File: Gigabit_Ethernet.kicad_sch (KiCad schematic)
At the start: 1 part, among them X800 ECS-2520MV-250-BN-TR

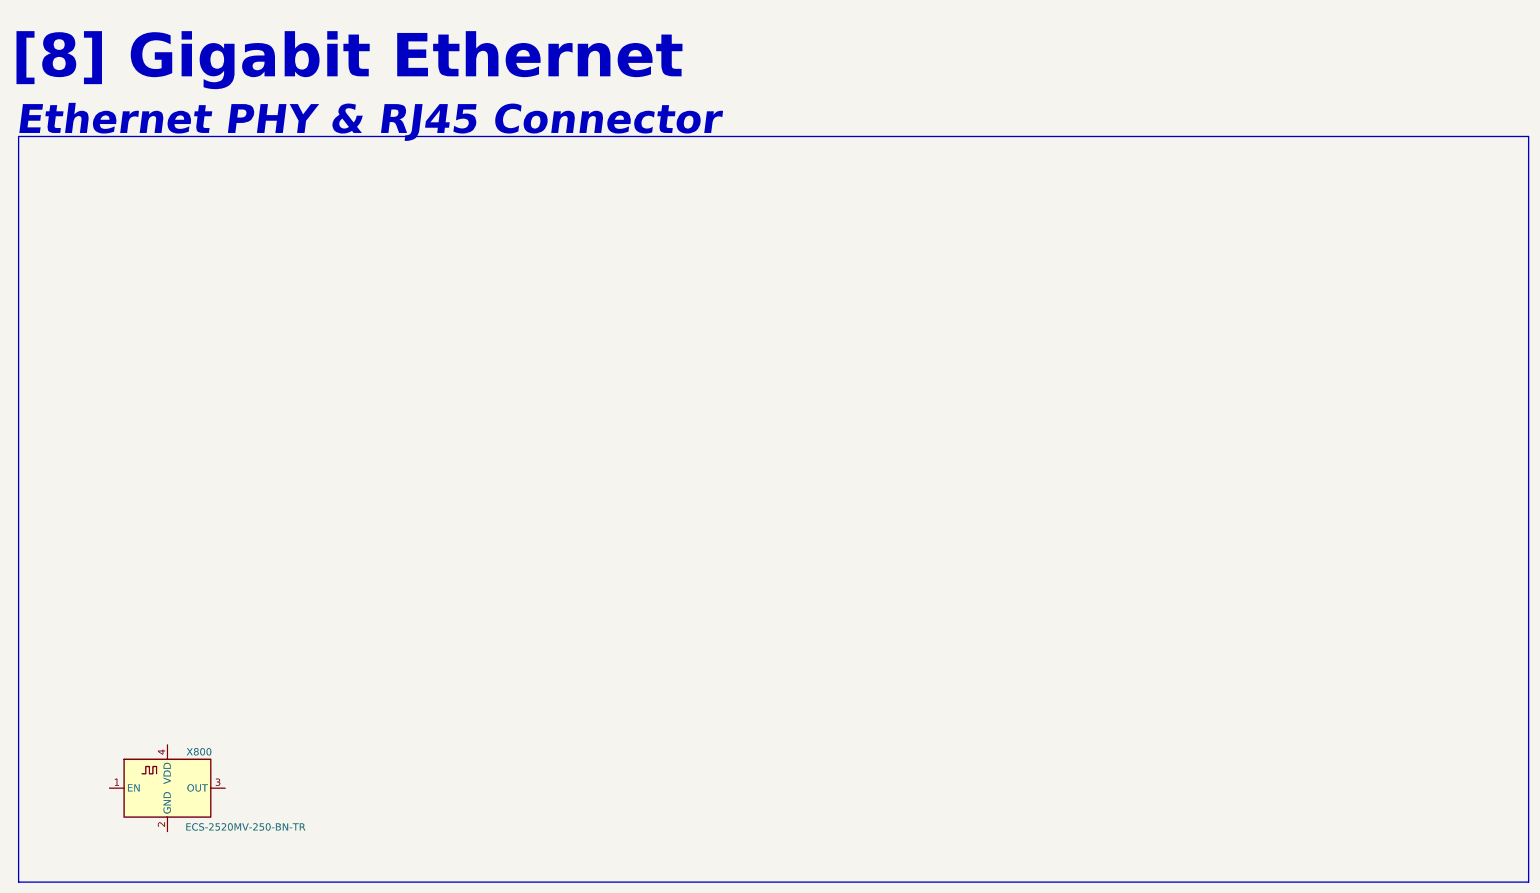
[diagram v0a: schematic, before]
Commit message: Completed page 8, Gigabit Ethernet Controller
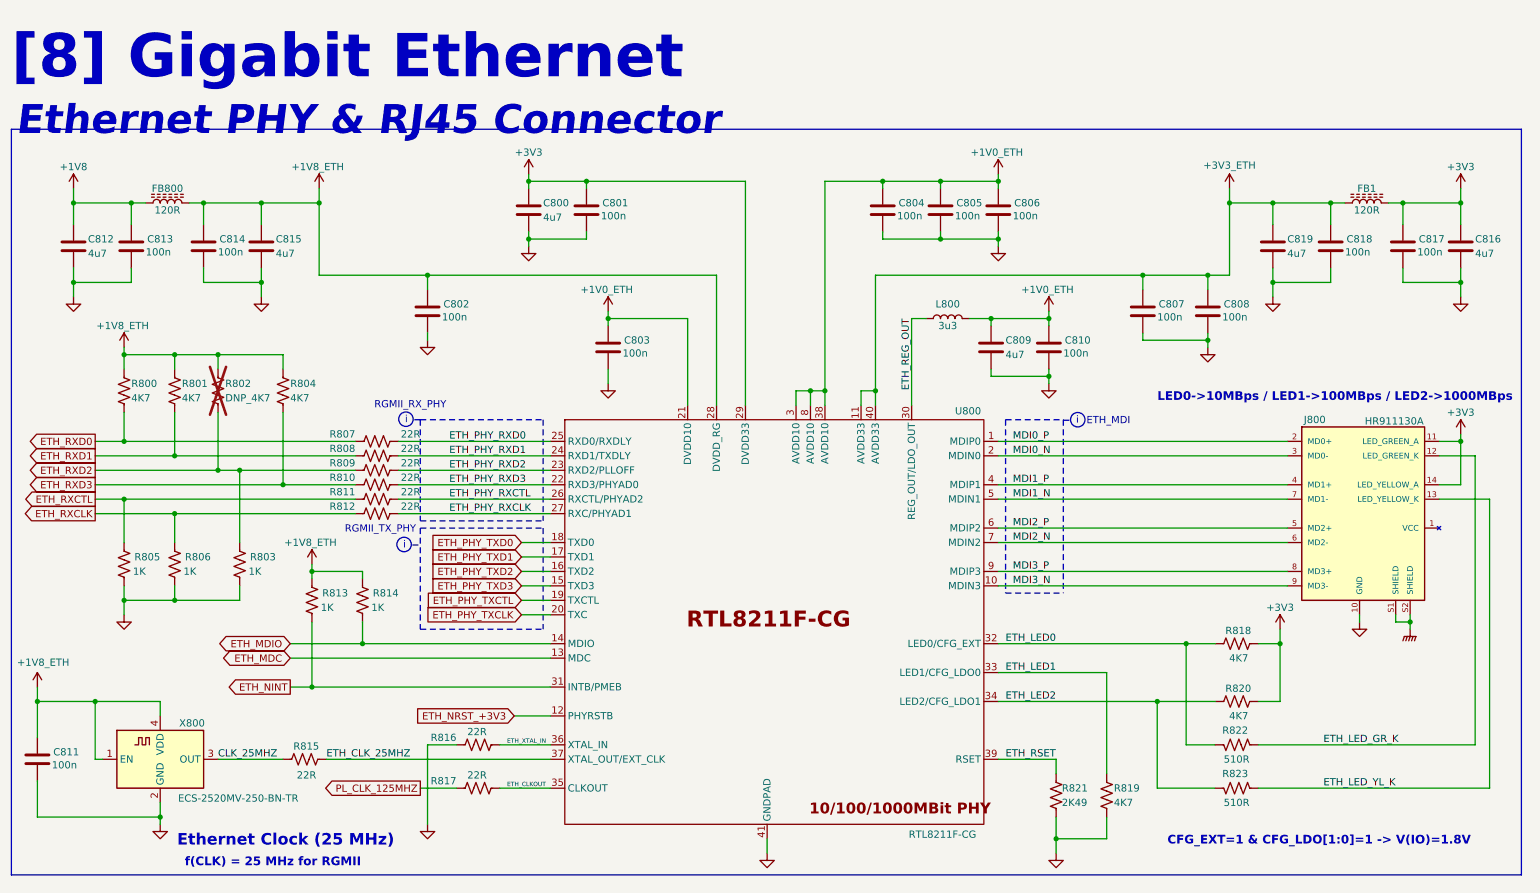
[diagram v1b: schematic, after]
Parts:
- added C800, C809, C812, C815, C816, C819: 4u7, Capacitor_SMD:C_0402_1005Metric, symbol Device:C
- added C801, C802, C803, C804, C805, C806, C807, C808, C810, C811, C813, C814, C817, C818: 100n, Capacitor_SMD:C_0402_1005Metric, symbol Device:C
- added FB1, FB800: 120R, Inductor_SMD:L_0402_1005Metric, symbol Device:L_Ferrite
- added J800: HR911130A, ZeBra_footprints:HANRUN_HR911130A, symbol ZeBra-X:HR911130A
- added L800: 3u3, Inductor_SMD:L_0603_1608Metric, symbol Device:L
- added R800, R801, R804, R818, R819, R820: 4K7, Resistor_SMD:R_0402_1005Metric, symbol Device:R_US
- added R802: DNP_4K7, Resistor_SMD:R_0402_1005Metric, symbol Device:R_US
- added R803, R805, R806, R813, R814: 1K, Resistor_SMD:R_0402_1005Metric, symbol Device:R_US
- added R807, R808, R809, R810, R811, R812, R815, R816, R817: 22R, Resistor_SMD:R_0402_1005Metric, symbol Device:R_US
- added R821: 2K49, Resistor_SMD:R_0402_1005Metric, symbol Device:R_US
- added R822, R823: 510R, Resistor_SMD:R_0402_1005Metric, symbol Device:R_US
- added U800: RTL8211F-CG, Package_DFN_QFN:QFN-40-1EP_5x5mm_P0.4mm_EP3.8x3.8mm, symbol ZeBra-X:RTL8211F-CG
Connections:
- net +1V8_ETH: now reaches X800.1 (EN)
- net +1V8_ETH: now also X800.4 (VDD), C802.1, C811.1, C814.1, C815.1, FB800.2, R800.1, R801.1, R802.1, R804.1, R813.2, R814.2, U800.28 (DVDD_RG)
- net GND: now reaches X800.2 (GND)
- net GND: now also C800.2, C801.2, C802.2, C803.2, C804.2, C805.2, C806.2, C807.2, C808.2, C809.2, C810.2, C811.2, C812.2, C813.2, C814.2, C815.2, C816.2, C817.2, C818.2, C819.2, J800.10 (GND), R803.1, R805.1, R806.1, R816.1, R819.2, R821.2, U800.41 (GNDPAD)
- net CLK_25MHZ: now reaches X800.3 (OUT)
- net CLK_25MHZ: now also R815.1
- new net +1V0_ETH: C803.1, C804.1, C805.1, C806.1, C809.1, C810.1, L800.2, U800.21 (DVDD10), U800.3 (AVDD10), U800.38 (AVDD10), U800.8 (AVDD10)
- new net +1V8: C812.1, C813.1, FB800.1
- new net +3V3: C800.1, C801.1, C816.1, C817.1, FB1.2, J800.11 (LED_GREEN_A), J800.14 (LED_YELLOW_A), R818.2, R820.2, U800.29 (DVDD33)
- new net +3V3_ETH: C807.1, C808.1, C818.1, C819.1, FB1.1, U800.11 (AVDD33), U800.40 (AVDD33)
- new net ETH_CLKOUT: R817.2, U800.35 (CLKOUT)
- new net ETH_CLK_25MHZ: R815.2, U800.37 (XTAL_OUT/EXT_CLK)
- new net ETH_LED0: R818.1, R822.2, U800.32 (LED0/CFG_EXT)
- new net ETH_LED1: R819.1, U800.33 (LED1/CFG_LDO0)
- new net ETH_LED2: R820.1, R823.2, U800.34 (LED2/CFG_LDO1)
- new net ETH_LED_GR_K: J800.12 (LED_GREEN_K), R822.1
- new net ETH_LED_YL_K: J800.13 (LED_YELLOW_K), R823.1
- new net ETH_MDC: U800.13 (MDC)
- new net ETH_MDIO: R814.1, U800.14 (MDIO)
- new net ETH_NINT: R813.1, U800.31 (INTB/PMEB)
- new net ETH_NRST_+3V3: U800.12 (PHYRSTB)
- new net ETH_PHY_RXCLK: R812.2, U800.27 (RXC/PHYAD1)
- new net ETH_PHY_RXCTL: R811.2, U800.26 (RXCTL/PHYAD2)
- new net ETH_PHY_RXD0: R807.2, U800.25 (RXD0/RXDLY)
- new net ETH_PHY_RXD1: R808.2, U800.24 (RXD1/TXDLY)
- new net ETH_PHY_RXD2: R809.2, U800.23 (RXD2/PLLOFF)
- new net ETH_PHY_RXD3: R810.2, U800.22 (RXD3/PHYAD0)
- new net ETH_PHY_TXCLK: U800.20 (TXC)
- new net ETH_PHY_TXCTL: U800.19 (TXCTL)
- new net ETH_PHY_TXD0: U800.18 (TXD0)
- new net ETH_PHY_TXD1: U800.17 (TXD1)
- new net ETH_PHY_TXD2: U800.16 (TXD2)
- new net ETH_PHY_TXD3: U800.15 (TXD3)
- new net ETH_REG_OUT: L800.1, U800.30 (REG_OUT/LDO_OUT)
- new net ETH_RSET: R821.1, U800.39 (RSET)
- new net ETH_RXCLK: R806.2, R812.1
- new net ETH_RXCTL: R805.2, R811.1
- new net ETH_RXD0: R800.2, R807.1
- new net ETH_RXD1: R801.2, R808.1
- new net ETH_RXD2: R802.2, R803.2, R809.1
- new net ETH_RXD3: R804.2, R810.1
- new net ETH_XTAL_IN: R816.2, U800.36 (XTAL_IN)
- new net GNDPWR: J800.S1 (SHIELD), J800.S2 (SHIELD)
- new net MDI0_N: J800.3 (MD0-), U800.2 (MDIN0)
- new net MDI0_P: J800.2 (MD0+), U800.1 (MDIP0)
- new net MDI1_N: J800.7 (MD1-), U800.5 (MDIN1)
- new net MDI1_P: J800.4 (MD1+), U800.4 (MDIP1)
- new net MDI2_N: J800.6 (MD2-), U800.7 (MDIN2)
- new net MDI2_P: J800.5 (MD2+), U800.6 (MDIP2)
- new net MDI3_N: J800.9 (MD3-), U800.10 (MDIN3)
- new net MDI3_P: J800.8 (MD3+), U800.9 (MDIP3)
- new net PL_CLK_125MHZ: R817.1
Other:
- note added: "CFG_EXT=1 & CFG_LDO[1:0]=1 -> V(IO)=1.8V"
- note added: "ETH_MDI"
- note added: "Ethernet Clock (25 MHz)"
- note added: "LED0->10MBps / LED1->100MBps / LED2->1000MBps"
- note added: "RGMII_RX_PHY"
- note added: "RGMII_TX_PHY"
- note added: "f(CLK) = 25 MHz for RGMII"
- note added: "i"
- moved on the sheet: X800

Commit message: started page 9, USB2.0 hub
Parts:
- X800: Distributor Link (none) -> https://www.digikey.com/en/products/detail/ecs-inc/ecs-2520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; Manufacturer (none) -> ECS; Manufacturer PN (none) -> ECS-2520MV-250-BN-TR
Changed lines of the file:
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@@
 	)
 	(symbol
-		(lib_name "ZeBra-X:RTL8211F-CG")
 		(lib_id "ZeBra-X:RTL8211F-CG")
 		(at 146.05 104.14 0)
@@
 			)
 		)
-		(property "Description" "HCMOS Crystal Clock Oscillator, 2.5x2.0 mm SMD"
+		(property "Description" "XTAL OSC XO 25.0000MHZ CMOS SMD"
 			(at 39.37 144.78 0)
 			(effects
+				(font
+					(size 1.27 1.27)
+				)
+				(hide yes)
+			)
+		)
+		(property "Distributor Link" "https://www.digikey.com/en/products/detail/ecs-inc/ecs-2520mv-250-bn-tr/8593607?_gl=1*pkc9pi*_up*MQ..*_gs*MQ..&gclid=Cj0KCQiAv628BhC2ARIsAIJIiK_gC5z4fVgKeGw85gbylbf80bbv2gx8Tdjn1h0ffjvb1ZfNebJjHEwaAgYrEALw_wcB&gclsrc=aw.ds"
+			(at 39.37 144.78 0)
+			(effects
+				(font
+					(size 1.27 1.27)
+				)
+				(hide yes)
+			)
+		)
+		(property "Manufacturer" "ECS"
+			(at 39.37 144.78 0)
+			(effects
+				(font
+					(size 1.27 1.27)
+				)
+				(hide yes)
+			)
+		)
+		(property "Manufacturer PN" "ECS-2520MV-250-BN-TR"
+			(at 39.37 144.78 0)
+			(effects
